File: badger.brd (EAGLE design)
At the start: 149.2 x 68.3 mm, 44 parts, among them Q1 MOSFET-NCHANNEL2N7002PW, U1 NCP1402

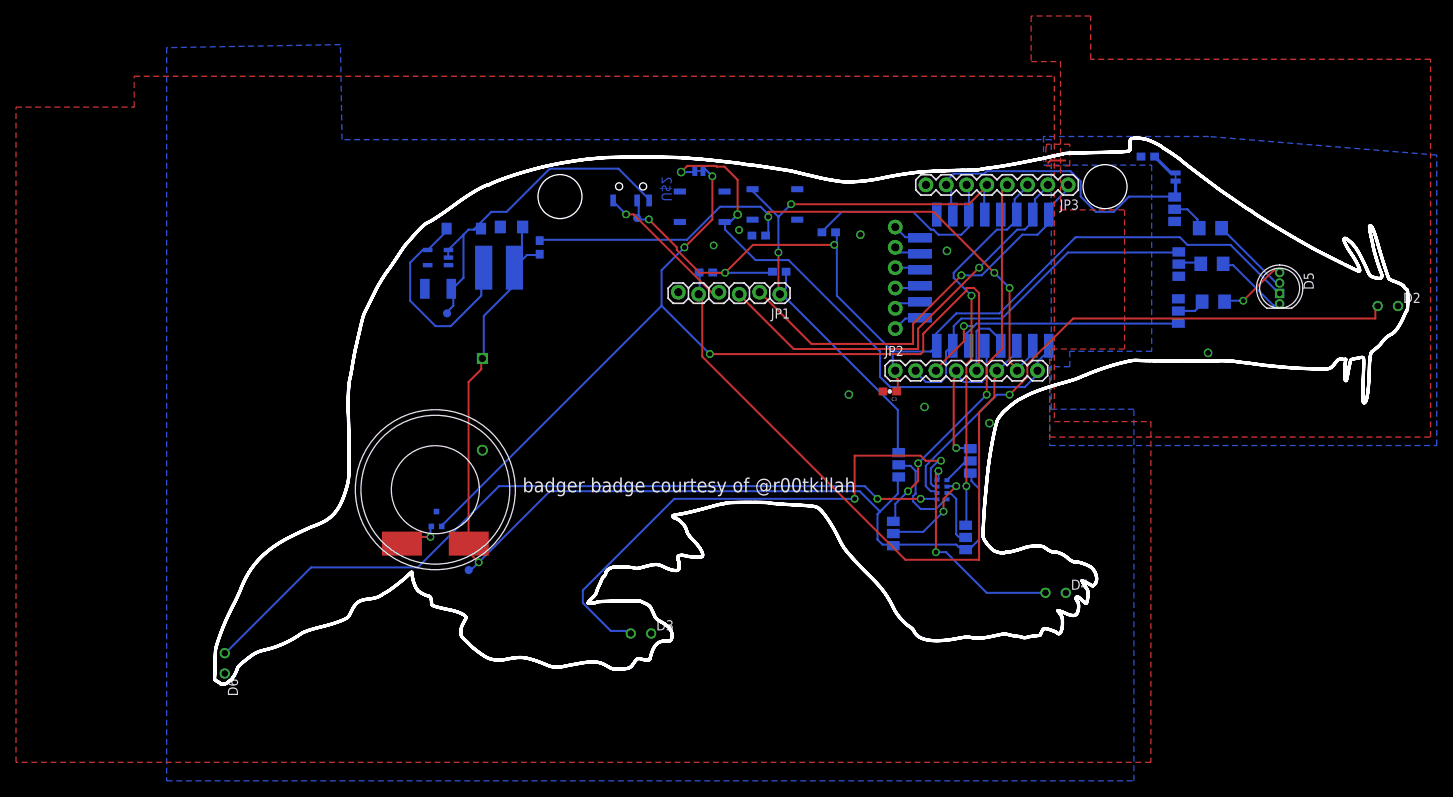
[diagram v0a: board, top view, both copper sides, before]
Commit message: Fix #3
All headers now locking
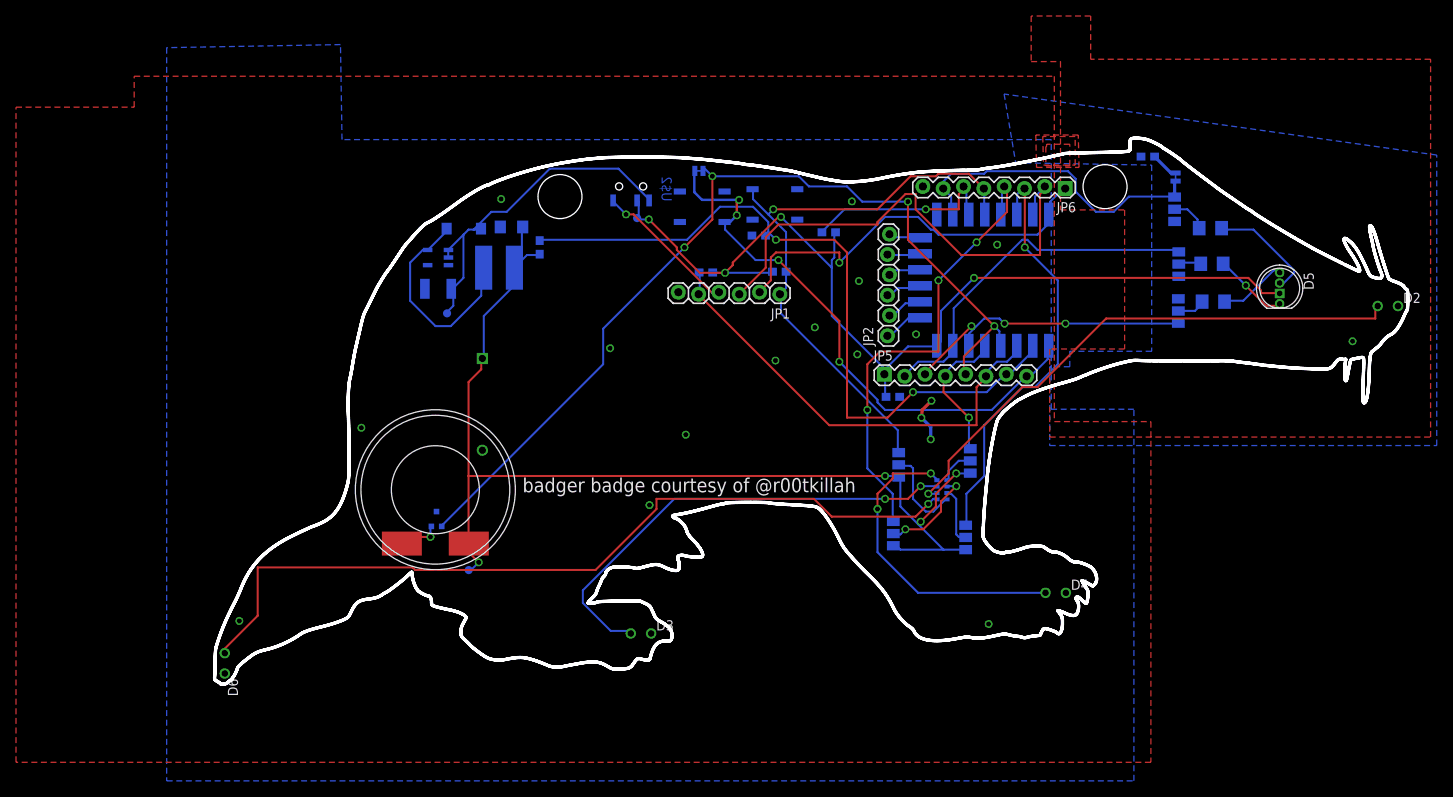
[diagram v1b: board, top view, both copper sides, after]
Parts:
- removed JP3: (no value), SparkFun-Connectors:1X08_ROUND
- removed JP4: (no value), SparkFun-Connectors:1X06
- added JP5, JP6: (no value), SparkFun-Connectors:1X08_LOCK
- JP2: device SparkFun-Connectors:1X08_ROUND -> SparkFun-Connectors:1X06_LOCK
- moved JP2 4.47 mm to (84.1, 43.6), turned to 90 degrees
- moved C3 0.78 mm to (84.8, 35.9), flipped to the bottom
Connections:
- net 3.3V: now also JP5.1; no longer JP2.1
- net ADC: now also JP5.7; no longer JP2.7
- net CH_PD: now also JP5.6; no longer JP2.6
- net CS0: now also JP2.1; no longer JP4.1
- net GND: now also JP6.8; no longer JP3.8
- net GPIO0: now also JP6.5; no longer JP3.5
- net GPIO10: now also JP2.4; no longer JP4.4
- net GPIO12: now also JP5.3; no longer JP2.3
- net GPIO13: now also JP5.2; no longer JP2.2
- net GPIO14: now also JP5.4; no longer JP2.4
- net GPIO15: now also JP6.7; no longer JP3.7
- net GPIO16: now also JP5.5; no longer JP2.5
- net GPIO2: now also JP6.6; no longer JP3.6
- net GPIO4: now also JP6.4; no longer JP3.4
- net GPIO5: now also JP6.3; no longer JP3.3
- net GPIO9: now also JP2.3; no longer JP4.3
- net MISO: now also JP2.2; no longer JP4.2
- net MOSI: now also JP2.5; no longer JP4.5
- net RESET: now also JP5.8; no longer JP2.8
- net RX: now also JP6.2; no longer JP3.2
- net SCLK: now also JP2.6; no longer JP4.6
- net TX: now also JP6.1; no longer JP3.1
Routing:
- net CH_PD: track 85.0 -> 57.4 mm
- net N$7: track 27.3 -> 39.6 mm
- net GPIO16: track 126.0 -> 115.7 mm, vias 3 -> 4
- net N$6: track 68.9 -> 58.9 mm
- net ADC: track 83.4 -> 92.9 mm, vias 3 -> 2
- net RX: track 53.1 -> 62.5 mm, vias 1 -> 0
- net GPIO4: track 52.0 -> 58.6 mm
- net N$11: track 98.3 -> 103.7 mm, vias 2 -> 1
- net GPIO5: track 48.7 -> 53.3 mm, vias 2 -> 1
- net N$8: track 10.5 -> 14.2 mm
- net 3.3V: track 120.7 -> 124.2 mm, vias 3 -> 4
- net GND: track 2.24 -> 5.79 mm, vias 8 -> 18
- net GPIO14: track 20.7 -> 18.0 mm
- net TX: track 52.7 -> 50.4 mm
- net N$5: track 70.8 -> 68.7 mm
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- added copper zone on layer 1, net N$10

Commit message: as sent to oshpark for proto
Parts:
- added D7: 250mA/100V, SparkFun-DiscreteSemi:SOD-323
- added LOGO1: OSHW-LOGOL-COPPER, SparkFun-Aesthetics:OSHW-LOGO-L_COPPER
- moved VIN 26.4 mm to (29.0, 40.5)
- moved R6 26.2 mm to (41.8, 55.9), turned to 90 degrees
- moved R5 3.48 mm to (41.8, 51.3)
- moved D6 1.88 mm to (2.20, 4.26), flipped to the bottom
- moved CHEAPO-4 1.41 mm to (120.1, 45.3)
- moved GPIO15<->GND 1.11 mm to (119.0, 63.4), turned to 0 degrees
- moved R10 0.99 mm to (90.1, 23.8)
- moved GPIO16<->RESET 0.64 mm to (61.1, 63.8), turned to 90 degrees
- moved JP2 0.59 mm to (84.2, 44.1), flipped to the bottom
- moved JP6 0.56 mm to (105.8, 61.8), flipped to the bottom, turned to 0 degrees
- moved JP1 0.43 mm to (71.0, 49.1), flipped to the bottom, turned to 0 degrees
- moved D4 0.32 mm to (105.4, 11.6), flipped to the bottom, turned to 180 degrees
- moved R3 0.31 mm to (70.3, 51.5)
- moved CHEAPO-5 0.31 mm to (120.2, 52.5), turned to 90 degrees
- moved JP5 0.19 mm to (83.7, 38.8), flipped to the bottom, turned to 180 degrees
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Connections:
- net GND: now also D7.A
- net N$18: now also D7.C
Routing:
- net N$7: track 39.6 -> 24.6 mm, vias 2 -> 1
- net ADC: track 92.9 -> 79.0 mm, vias 2 -> 0
- net VIN: track 135.6 -> 146.2 mm, vias 4 -> 0
- net RX: track 62.5 -> 53.0 mm
- net N$5: track 68.7 -> 77.8 mm, vias 1 -> 2
- net N$11: track 103.7 -> 95.7 mm, vias 1 -> 2
- net RESET: track 70.9 -> 62.8 mm, vias 4 -> 3
- net N$18: track 5.73 -> 13.7 mm
- net GPIO4: track 58.6 -> 51.6 mm, vias 3 -> 2
- net 3.3V: track 124.2 -> 117.6 mm, vias 4 -> 0
- net GND: track 5.79 -> 0.00 mm, vias 18 -> 17
- net GPIO16: track 115.7 -> 111.8 mm, vias 4 -> 3
- net GPIO13: track 45.2 -> 41.5 mm, vias 0 -> 2
- net TX: track 50.4 -> 53.4 mm
- net GPIO2: track 25.5 -> 22.7 mm
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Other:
- outline, holes or cut-outs redrawn
- board text added: "BLACK"
- board text added: "CHEAP"

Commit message: fix #8
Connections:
- net GND: now also JP1.6
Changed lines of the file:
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@@
 <via x="87.20343125" y="32.06150625" extent="1-16" drill="0.6"/>
 <via x="88.07256875" y="36.407190625" extent="1-16" drill="0.6"/>
+<contactref element="JP1" pad="6"/>
 <wire x1="90.280575" y1="58.706859375" x2="88.0616" y2="61.678309375" width="0" layer="19" extent="16-16"/>
 </signal>

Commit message: fix #7
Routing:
- net GND: track 0.00 -> 14.1 mm, vias 17 -> 20
- removed copper zone on layer 1, net N$10
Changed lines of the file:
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@@
 <layer number="17" name="Pads" color="2" fill="1" visible="yes" active="yes"/>
 <layer number="18" name="Vias" color="2" fill="1" visible="yes" active="yes"/>
-<layer number="19" name="Unrouted" color="6" fill="1" visible="yes" active="yes"/>
+<layer number="19" name="Unrouted" color="11" fill="1" visible="yes" active="yes"/>
 <layer number="20" name="Dimension" color="15" fill="1" visible="yes" active="yes"/>
 <layer number="21" name="tPlace" color="7" fill="1" visible="yes" active="yes"/>
@@
 <contactref element="C3" pad="2"/>
 <contactref element="R4" pad="1"/>
-<polygon width="0.4064" layer="1">
-<vertex x="104.006753125" y="67.213278125"/>
-<vertex x="103.91018125" y="67.213278125"/>
-<vertex x="103.91018125" y="64.79900625"/>
-<vertex x="106.903875" y="64.79900625"/>
-<vertex x="106.903875" y="67.502990625"/>
-<vertex x="104.006753125" y="67.502990625"/>
-</polygon>
 <contactref element="JP6" pad="8"/>
-<polygon width="0.4064" layer="1">
-<vertex x="103.62046875" y="64.895578125"/>
-<vertex x="107.579871875" y="64.895578125"/>
-<vertex x="107.579871875" y="68.468696875"/>
-<vertex x="103.523896875" y="68.468696875"/>
-</polygon>
 <contactref element="D7" pad="A"/>
 <via x="7.146240625" y="15.64446875" extent="1-16" drill="0.6"/>
@@
 <via x="88.07256875" y="36.407190625" extent="1-16" drill="0.6"/>
 <contactref element="JP1" pad="6"/>
-<wire x1="90.280575" y1="58.706859375" x2="88.0616" y2="61.678309375" width="0" layer="19" extent="16-16"/>
+<via x="92.0234625" y="54.26590625" extent="1-16" drill="0.6"/>
+<wire x1="106.41535625" y1="63.747625" x2="103.96026875" y2="63.747625" width="0.4064" layer="1"/>
+<wire x1="103.96026875" y1="63.747625" x2="103.96026875" y2="63.49365" width="0.4064" layer="1"/>
+<via x="82.626403125" y="61.969803125" extent="1-16" drill="0.6"/>
+<wire x1="105.907409375" y1="59.345396875" x2="105.82275" y2="59.345396875" width="0.4064" layer="1"/>
+<wire x1="105.82275" y1="59.345396875" x2="105.82275" y2="58.92210625" width="0.4064" layer="1"/>
+<wire x1="105.82275" y1="58.92210625" x2="105.23014375" y2="58.92210625" width="0.4064" layer="1"/>
+<wire x1="105.23014375" y1="58.92210625" x2="105.23014375" y2="57.906209375" width="0.4064" layer="1"/>
+<wire x1="105.23014375" y1="57.906209375" x2="104.637534375" y2="57.906209375" width="0.4064" layer="1"/>
+<wire x1="104.637534375" y1="57.906209375" x2="104.637534375" y2="57.48291875" width="0.4064" layer="1"/>
+<wire x1="90.280575" y1="58.706859375" x2="94.224578125" y2="58.706859375" width="0.4064" layer="16"/>
+<wire x1="94.224578125" y1="58.706859375" x2="94.224578125" y2="54.435221875" width="0.4064" layer="16"/>
+<via x="102.182446875" y="53.16535" extent="1-16" drill="0.6"/>
 </signal>
 <signal name="VIN">
@@
 <via x="20.0025" y="18.7325" extent="1-16" drill="0.6096"/>
 </signal>
-<signal name="N$10">
-<polygon width="0.4064" layer="1">
-<vertex x="102.654759375" y="68.6618375"/>
-<vertex x="102.75133125" y="64.605865625"/>
-<vertex x="108.062725" y="64.605865625"/>
-<vertex x="107.966153125" y="68.6618375"/>
-</polygon>
-</signal>
 </signals>

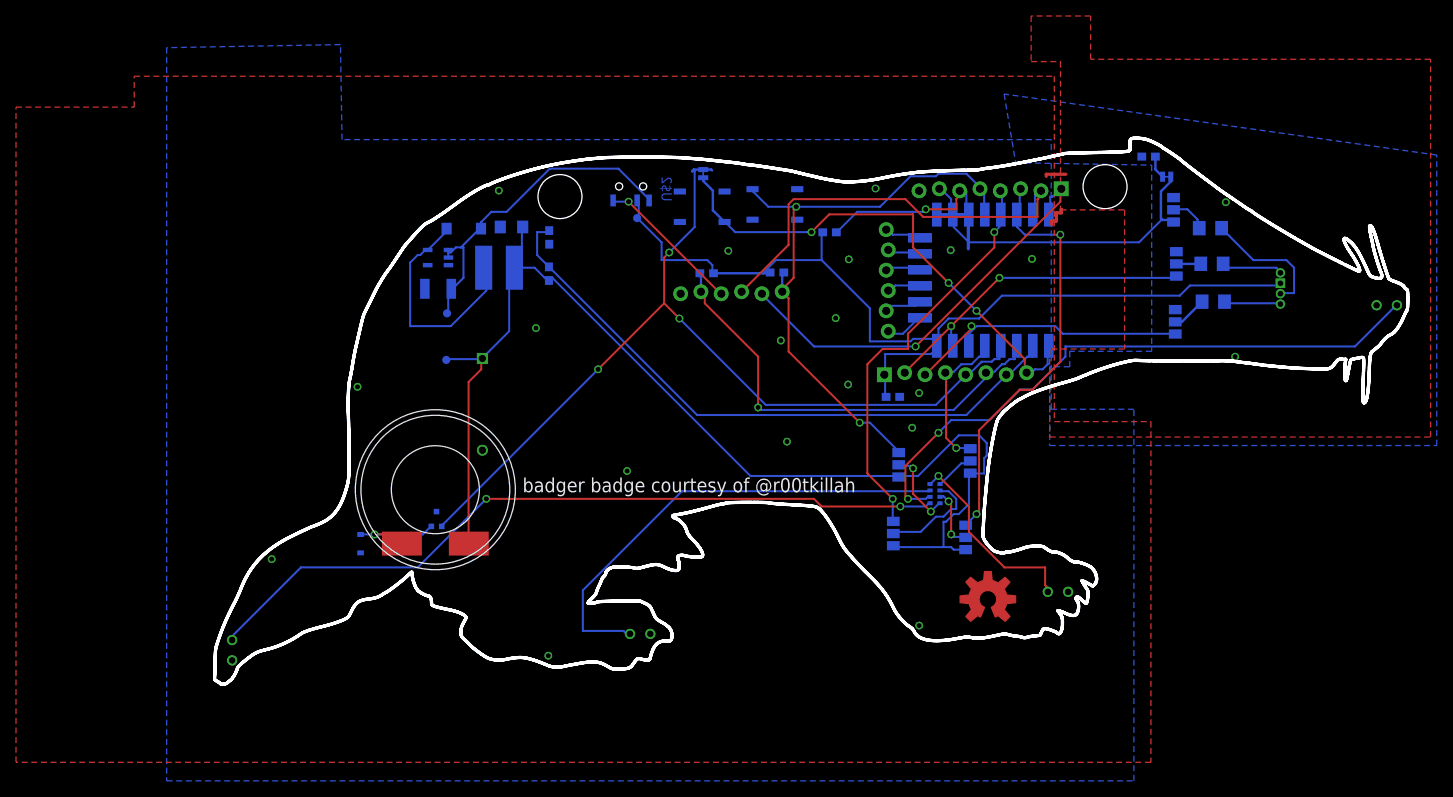
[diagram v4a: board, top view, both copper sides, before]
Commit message: Add 5mil dimension buffer; bring vias closer in; reroute
Signed-off-by: Hacker, J.R <r00tkillah@gmail.com>
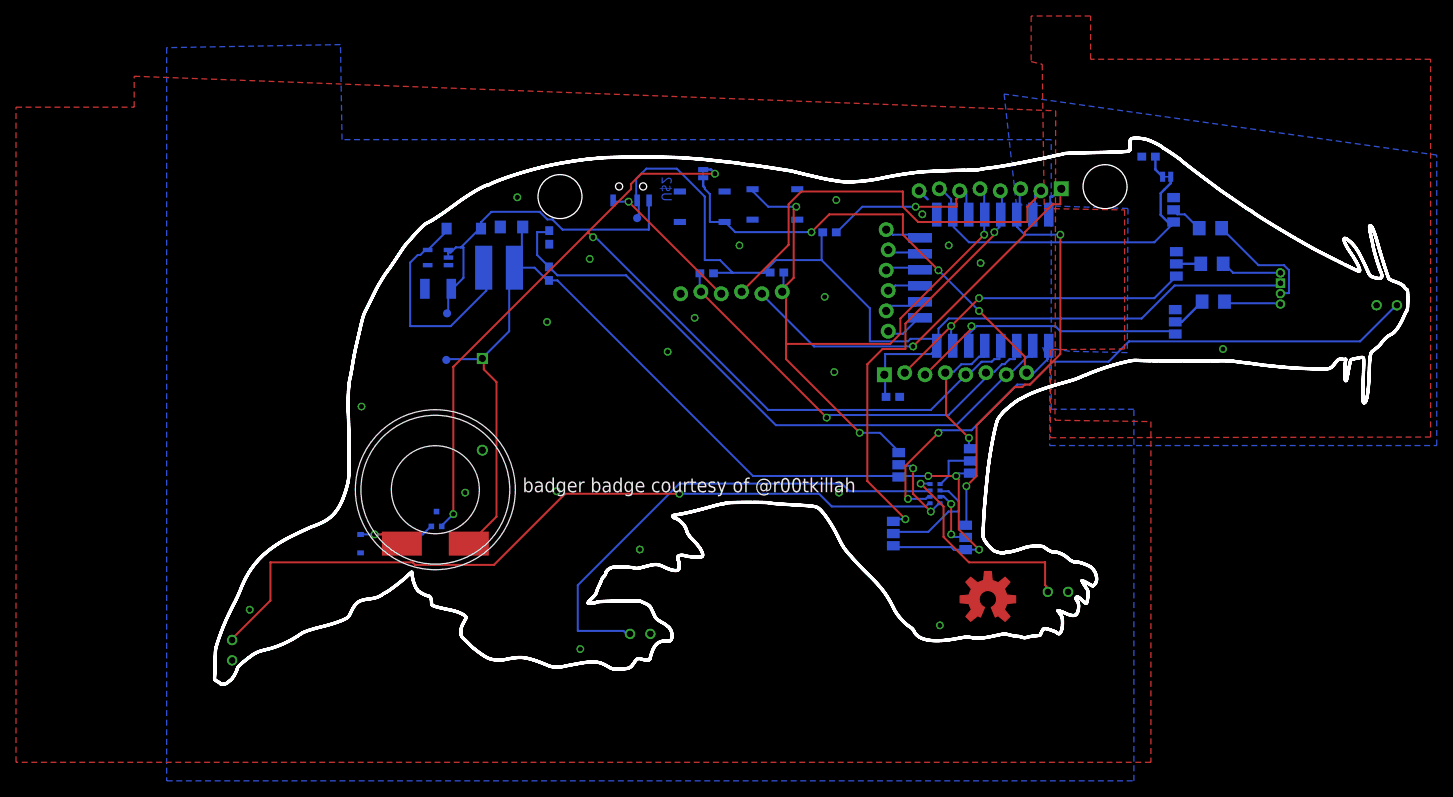
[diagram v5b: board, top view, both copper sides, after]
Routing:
- net GPIO16: track 111.8 -> 130.4 mm
- net GND: track 14.1 -> 1.52 mm
- net 3.3V: track 117.6 -> 128.7 mm
- net GPIO0: track 76.5 -> 87.3 mm, vias 2 -> 3
- net VIN: track 146.2 -> 137.8 mm, vias 0 -> 3
- net CH_PD: track 58.0 -> 54.5 mm
- net N$11: track 95.7 -> 98.8 mm, vias 2 -> 1
- net N$6: track 59.7 -> 62.1 mm
- net N$7: track 24.6 -> 26.9 mm
- net RX: track 53.0 -> 55.1 mm
- net GPIO4: track 51.6 -> 53.5 mm
- net N$8: track 16.0 -> 14.5 mm
- net N$15: track 5.02 -> 6.10 mm
- net ADC: track 79.0 -> 80.1 mm
- net GPIO15: track 41.3 -> 42.2 mm
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
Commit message: unrouted fixes
speaker/pin collision
add source bitmaps to repo
bsides logo now hi-res
oshpark logo
harmonize (mostly) silk placement and size
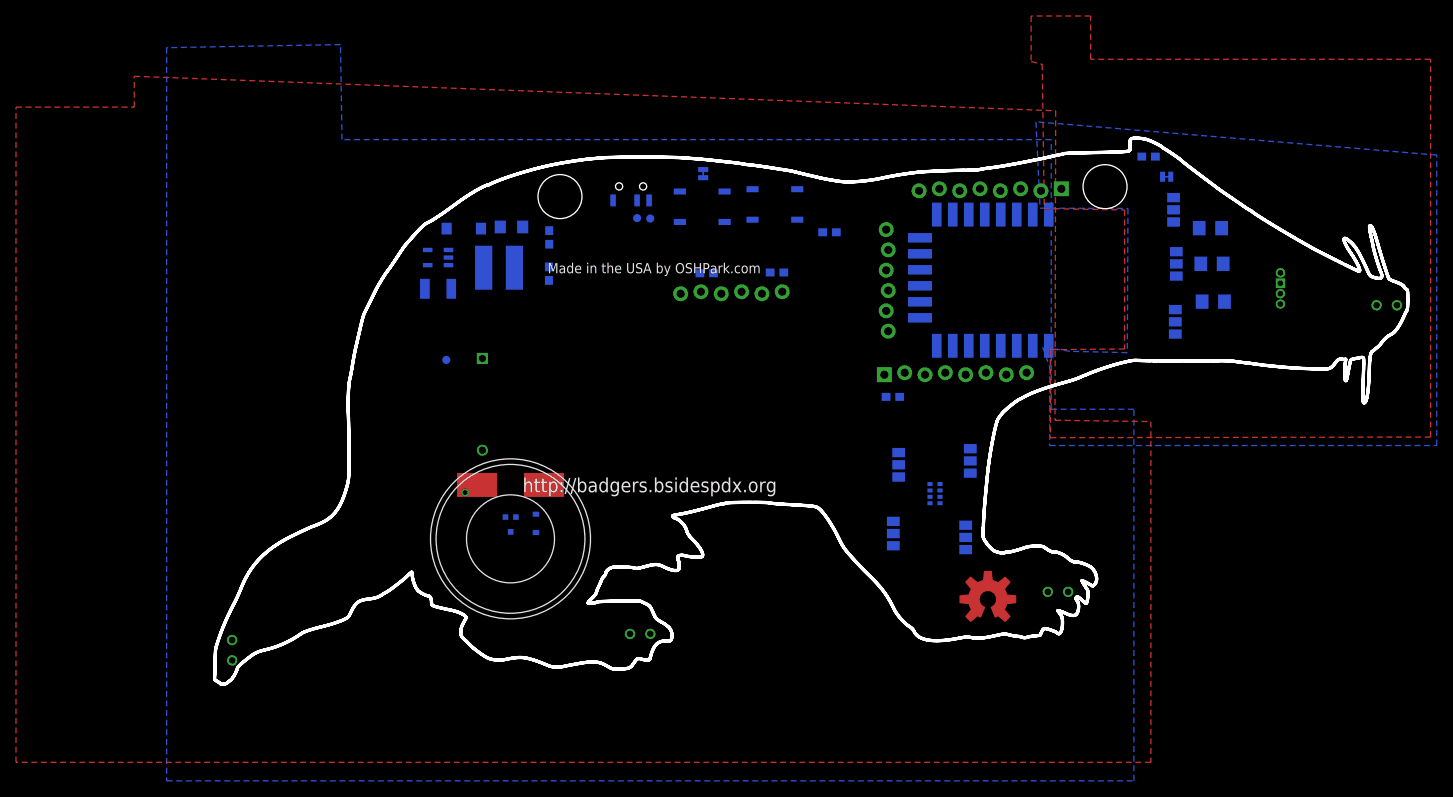
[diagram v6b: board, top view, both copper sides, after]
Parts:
- Q1: value MOSFET-NCHANNEL2N7002PW -> 2N7002PW
- moved VREG 28.0 mm to (54.5, 58.2)
- moved D7 22.1 mm to (40.2, 20.1)
- moved U$3 11.2 mm to (37.0, 18.2), turned to 180 degrees
- moved Q1 9.30 mm to (37.0, 20.0), turned to 180 degrees
- renumbered U$2 to S3
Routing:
- net VIN: track 137.8 -> 0.00 mm, vias 3 -> 0
- net GPIO16: track 130.4 -> 0.00 mm, vias 3 -> 0
- net 3.3V: track 128.7 -> 0.00 mm
- net N$11: track 98.8 -> 0.00 mm, vias 1 -> 0
- net GPIO0: track 87.3 -> 0.00 mm, vias 3 -> 0
- net ADC: track 80.1 -> 0.00 mm
- net N$5: track 76.9 -> 0.00 mm, vias 2 -> 0
- net RESET: track 63.0 -> 0.00 mm, vias 3 -> 0
- net N$6: track 62.1 -> 0.00 mm
- net RX: track 55.1 -> 0.00 mm
- net CH_PD: track 54.5 -> 0.00 mm, vias 1 -> 0
- net TX: track 53.8 -> 0.00 mm, vias 1 -> 0
- net GPIO4: track 53.5 -> 0.00 mm, vias 2 -> 0
- net GPIO5: track 53.2 -> 0.00 mm, vias 2 -> 0
- net VREG: track 42.8 -> 0.00 mm
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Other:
- board text added: "Made in the USA by OSHPark.com"
- board text added: "VFTDI"
- board text added: "http://badgers.bsidespdx.org"
- board text removed: "badger badge courtesy of @r00tkillah"

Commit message: routed
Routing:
- net VIN: track 0.00 -> 129.5 mm, vias 0 -> 2
- net GPIO16: track 0.00 -> 115.7 mm, vias 0 -> 4
- net 3.3V: track 0.00 -> 115.2 mm, vias 0 -> 4
- net N$11: track 0.00 -> 100.0 mm, vias 0 -> 1
- net N$5: track 0.00 -> 96.5 mm, vias 0 -> 2
- net ADC: track 0.00 -> 79.8 mm, vias 0 -> 2
- net GPIO0: track 0.00 -> 73.1 mm, vias 0 -> 2
- net RESET: track 0.00 -> 62.7 mm, vias 0 -> 3
- net N$6: track 0.00 -> 62.2 mm, vias 0 -> 2
- net TX: track 0.00 -> 60.3 mm
- net CH_PD: track 0.00 -> 55.8 mm, vias 0 -> 1
- net GPIO4: track 0.00 -> 54.0 mm
- net GPIO5: track 0.00 -> 51.0 mm, vias 0 -> 2
- net RX: track 0.00 -> 47.5 mm, vias 0 -> 2
- net GPIO15: track 0.00 -> 42.2 mm
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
